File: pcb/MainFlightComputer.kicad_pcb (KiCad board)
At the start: 4 copper layers, 50 x 50 mm, 74 parts, among them J1 614105150721, J3 Micro_SD_Card, J4 Pinout, J5 Debug, SW1 B3U-1000P, SW2 B3U-1000P, U1 STM32H533VET6, U2 MCP2221A-I/ST, U3 AP2112K-3.3

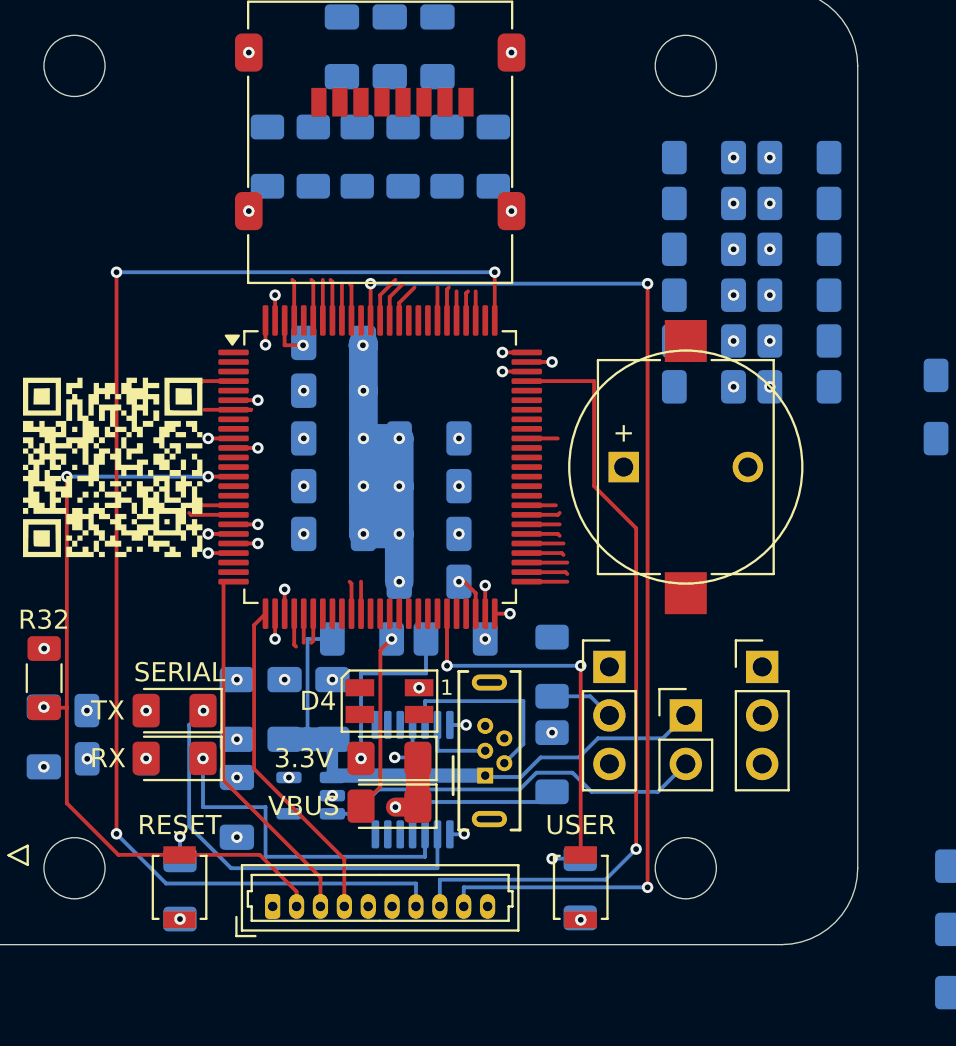
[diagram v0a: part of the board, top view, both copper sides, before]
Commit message: Routed `serial_tx` and `serial_rx`.
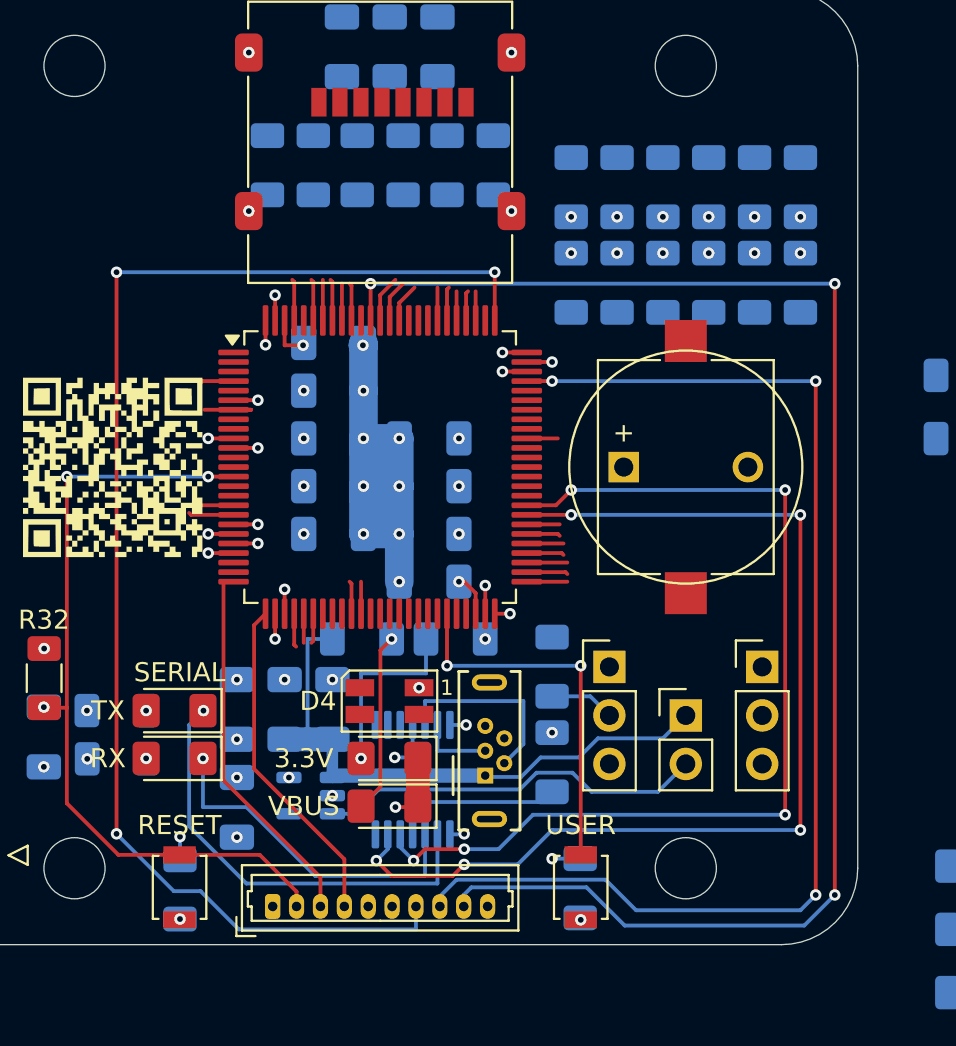
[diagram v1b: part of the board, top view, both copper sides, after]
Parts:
- moved R31 13.1 mm to (160.0, 90.3), turned to 90 degrees
- moved R22 12.6 mm to (160.0, 85.3), turned to -90 degrees
- moved R30 10.0 mm to (162.4, 90.3), turned to 90 degrees
- moved R25 9.25 mm to (162.4, 85.3), turned to -90 degrees
- moved R29 7.18 mm to (164.8, 90.3), turned to 90 degrees
- moved R26 6.55 mm to (172.0, 90.3), turned to 90 degrees
- moved R20 6.05 mm to (164.8, 85.3), turned to -90 degrees
- moved R24 5.28 mm to (172.0, 85.3), turned to -90 degrees
- moved R28 5.06 mm to (167.2, 90.3), turned to 90 degrees
- moved R27 4.77 mm to (169.6, 90.3), turned to 90 degrees
- moved R21 3.26 mm to (167.2, 85.3), turned to -90 degrees
- moved R23 2.78 mm to (169.6, 85.3), turned to -90 degrees
- moved R1 0.45 mm to (144.1, 84.2)
- moved R2 0.45 mm to (151.2, 84.2)
- moved R3 0.45 mm to (153.5, 84.2)
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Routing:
- net serial_rx: track 1.77 -> 56.0 mm, vias 0 -> 5
- net serial_tx: track 1.52 -> 53.0 mm, vias 0 -> 5
- net swdio: track 41.3 -> 63.6 mm, vias 1 -> 3
- net swo: track 58.6 -> 79.9 mm
- net /SERIAL_TX_ACTIVITY: track 22.1 -> 23.2 mm
- net swclk: track 69.7 -> 70.7 mm

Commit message: Routed `led_channel_x`.
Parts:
- moved R12 49.9 mm to (134.8, 106.0), turned to 90 degrees
- moved R13 47.0 mm to (139.4, 106.0), turned to 90 degrees
- moved R11 46.6 mm to (137.1, 106.0), turned to 90 degrees
- moved G*** 14.2 mm to (136.0, 85.8)
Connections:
- U1 pad 1: unconnected-(U1-PE2-Pad1) -> led_channel_red
- U1 pad 2: unconnected-(U1-PE3-Pad2) -> led_channel_green
- U1 pad 29: led_channel_red -> unconnected-(U1-PA4-Pad29)
- U1 pad 3: unconnected-(U1-PE4-Pad3) -> led_channel_blue
- U1 pad 30: led_channel_green -> unconnected-(U1-PA5-Pad30)
- U1 pad 31: led_channel_blue -> unconnected-(U1-PA6-Pad31)
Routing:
- net /DEBUG_LED_G_CATHODE: track 0.00 -> 18.6 mm, vias 0 -> 1
- net /DEBUG_LED_B_CATHODE: track 0.00 -> 17.3 mm, vias 0 -> 1
- net led_channel_green: track 1.53 -> 17.5 mm, vias 0 -> 3
- net led_channel_red: track 1.77 -> 17.7 mm, vias 0 -> 3
- net /DEBUG_LED_R_CATHODE: track 0.00 -> 15.8 mm, vias 0 -> 1
- net led_channel_blue: track 1.57 -> 12.4 mm, vias 0 -> 1
- net +3.3V: track 14.4 -> 13.5 mm, vias 37 -> 36
- net swclk: track 70.7 -> 69.9 mm

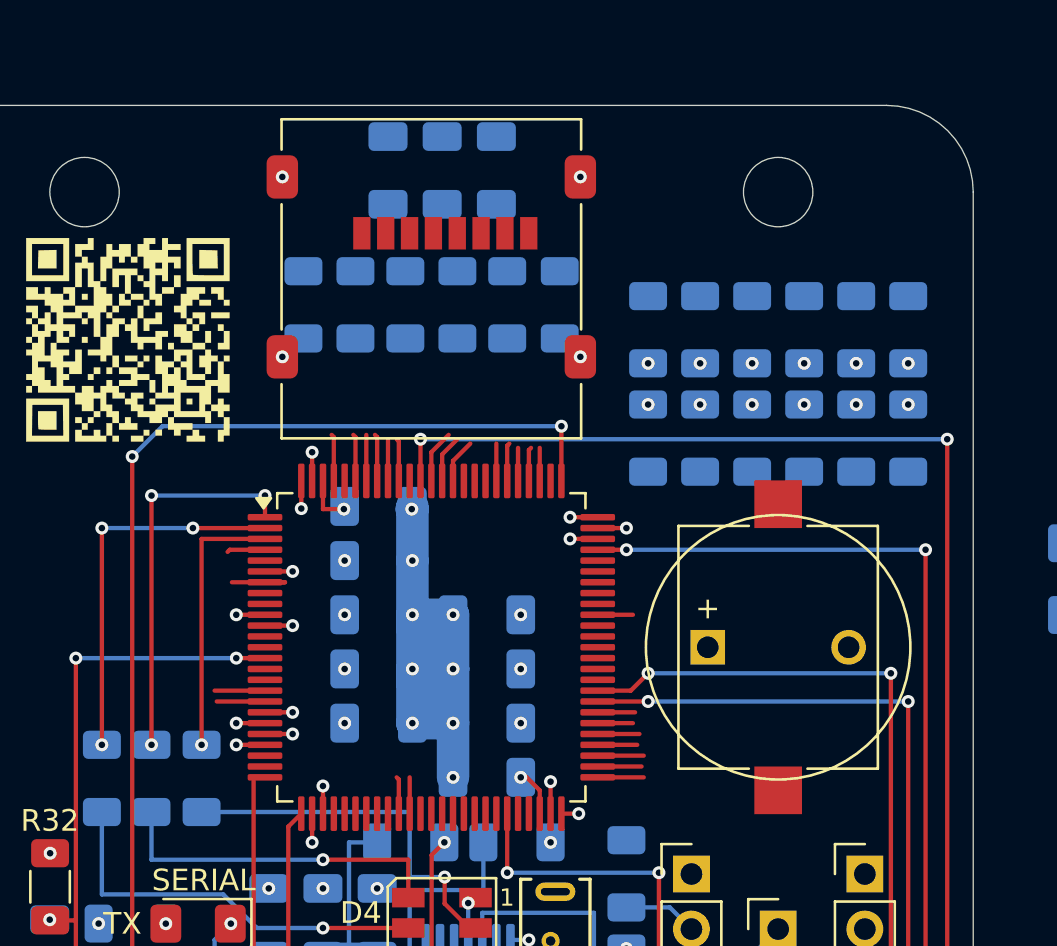
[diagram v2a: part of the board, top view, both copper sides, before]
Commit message: Routed uSD connector.
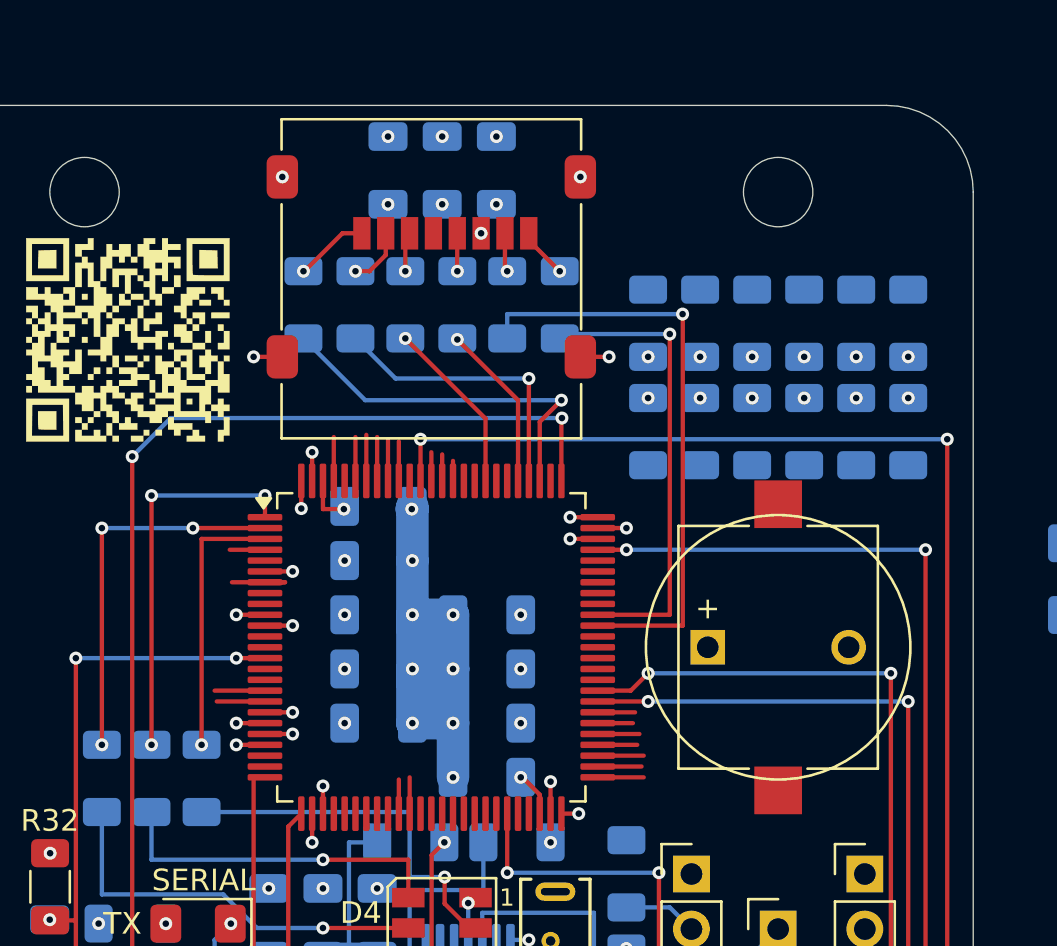
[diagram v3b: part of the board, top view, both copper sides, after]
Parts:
- moved R20 0.30 mm to (164.8, 85.0)
- moved R21 0.30 mm to (167.2, 85.0)
- moved R22 0.30 mm to (160.0, 85.0)
- moved R23 0.30 mm to (169.6, 85.0)
- moved R24 0.30 mm to (172.0, 85.0)
- moved R25 0.30 mm to (162.4, 85.0)
- moved R26 0.30 mm to (172.0, 90.0)
- moved R27 0.30 mm to (169.6, 90.0)
- moved R28 0.30 mm to (167.2, 90.0)
- moved R29 0.30 mm to (164.8, 90.0)
- moved R30 0.30 mm to (162.4, 90.0)
- moved R31 0.30 mm to (160.0, 90.0)
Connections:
- net Net-(J3-CLK) renamed /SD_CLK
- net Net-(J3-CMD) renamed /SD_CMD
- net Net-(J3-DAT0) renamed /SD_DAT0
- net Net-(J3-DAT1) renamed /SD_DAT1
- net Net-(J3-DAT2) renamed /SD_DAT2
- net Net-(J3-DAT3/CD) renamed /SD_DAT3
- U1 pad 37: sd_cmd -> unconnected-(U1-PB2-Pad37)
- U1 pad 52: sd_data_0 -> unconnected-(U1-PB13-Pad52)
- U1 pad 65: unconnected-(U1-PC8-Pad65) -> sd_data_0
- U1 pad 83: unconnected-(U1-PD2-Pad83) -> sd_cmd
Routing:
- net sd_data_0: track 2.02 -> 27.5 mm, vias 0 -> 1
- net sd_data_1: track 1.62 -> 21.4 mm, vias 0 -> 1
- net sd_data_2: track 1.53 -> 17.2 mm, vias 0 -> 1
- net sd_data_3: track 1.57 -> 13.5 mm, vias 0 -> 1
- net sd_cmd: track 0.00 -> 8.11 mm, vias 0 -> 1
- net sd_clock: track 1.53 -> 7.68 mm, vias 0 -> 1
- net /SD_DAT2: track 0.00 -> 3.42 mm, vias 0 -> 1
- net /SD_DAT3: track 0.00 -> 2.71 mm, vias 0 -> 1
- net GND: track 46.3 -> 49.0 mm, vias 32 -> 36
- net /SD_DAT1: track 0.00 -> 2.34 mm, vias 0 -> 1
- net unconnected-(U1-PB13-Pad52): track 0.00 -> 2.02 mm
- net /SD_CMD: track 0.00 -> 1.83 mm, vias 0 -> 1
- net /SD_DAT0: track 0.00 -> 1.82 mm, vias 0 -> 1
- net general_purpose_A: track 1.77 -> 0.00 mm
- net /SD_CLK: track 0.00 -> 1.75 mm, vias 0 -> 1
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
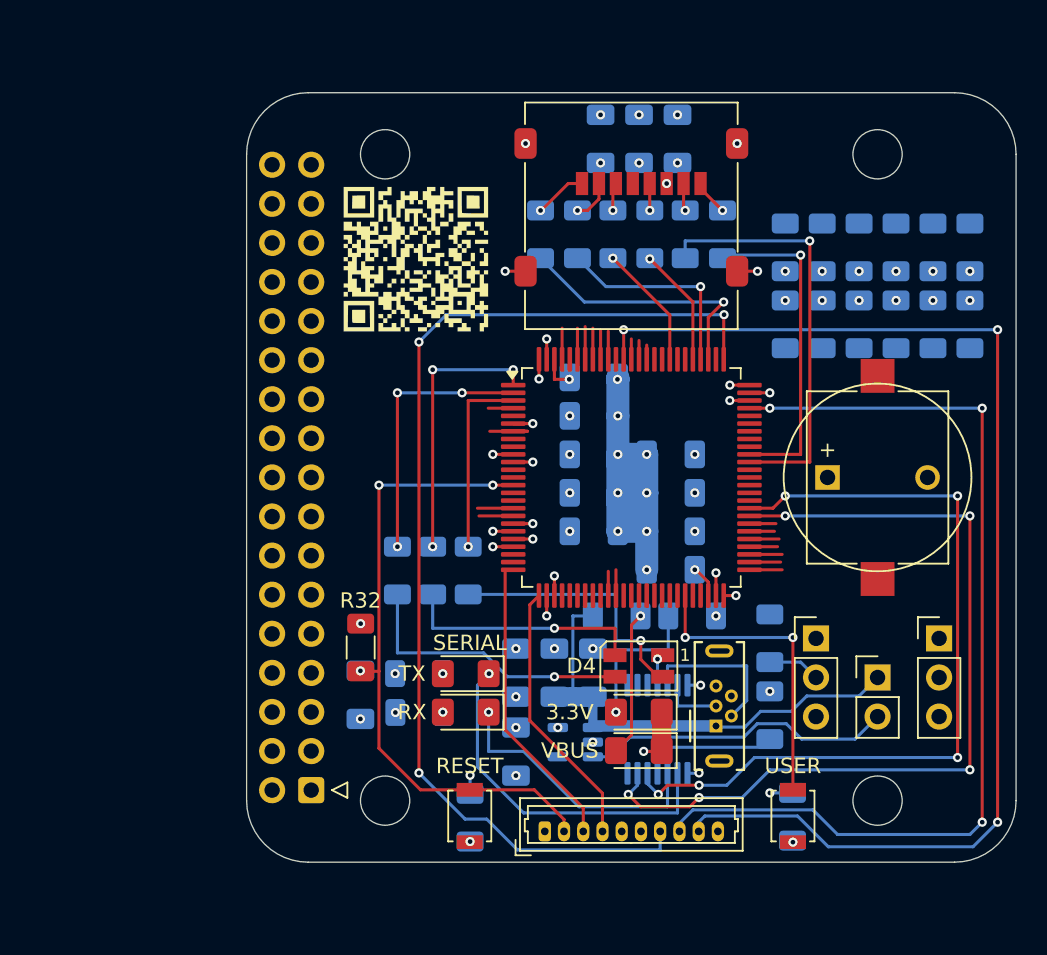
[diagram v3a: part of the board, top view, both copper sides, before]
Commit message: Using vertical IDC header instead of horizontal because it's cheaper.
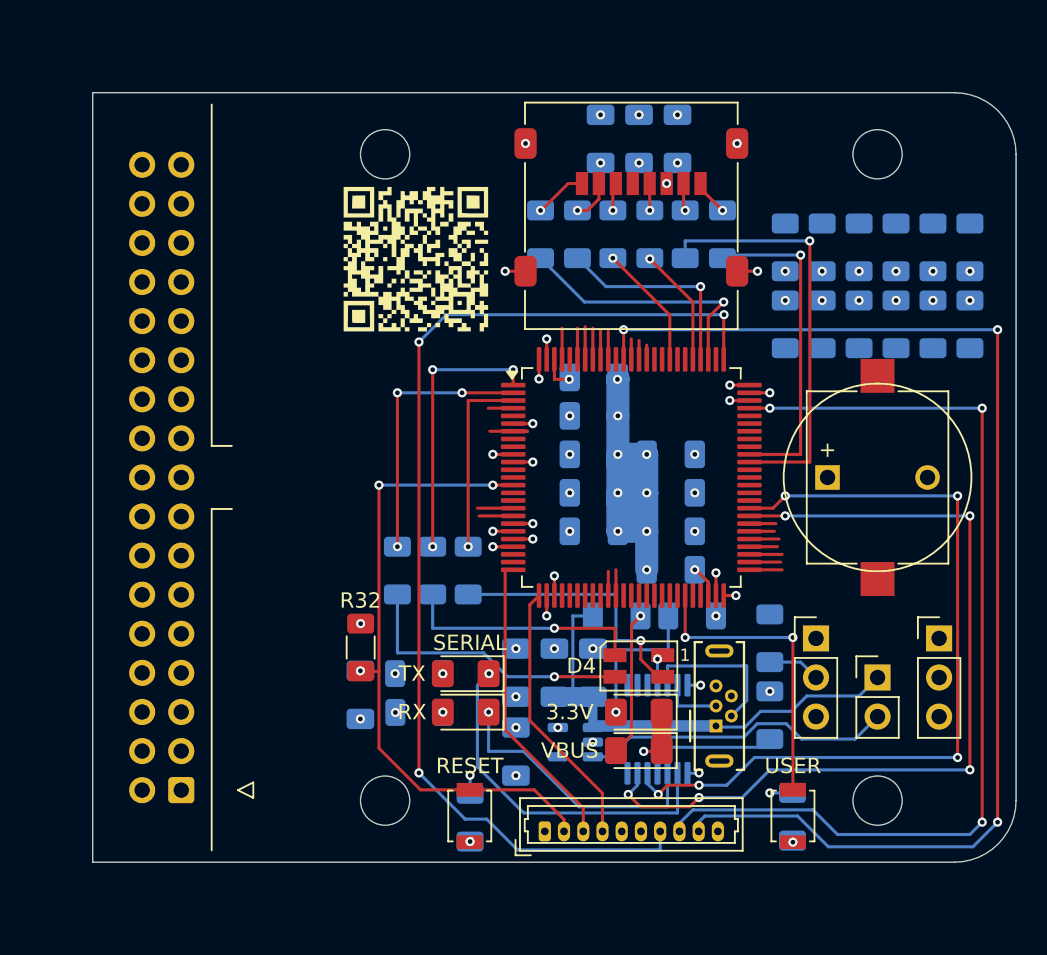
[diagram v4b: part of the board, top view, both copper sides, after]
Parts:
- J3: value Micro_SD_Card -> 0472192001
- J4: footprint pcb:IDC-Header_2x17_P2.54mm_Horizontal -> pcb:IDC-Header_2x17_P2.54mm_Vertical
- moved J4 8.44 mm to (120.8, 120.3)
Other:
- board size 50 x 50 mm -> 60 x 50 mm
